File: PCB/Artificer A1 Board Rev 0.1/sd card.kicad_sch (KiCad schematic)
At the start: 1 part

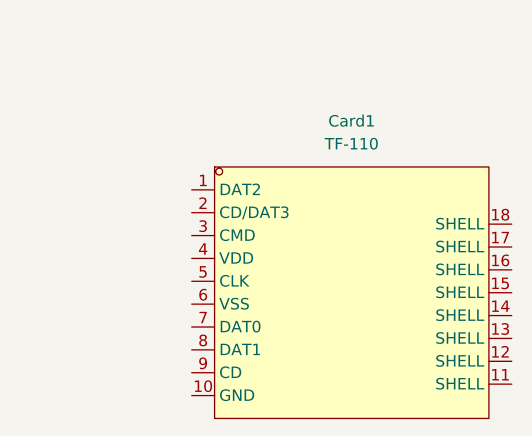
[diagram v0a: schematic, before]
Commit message: localized libraries
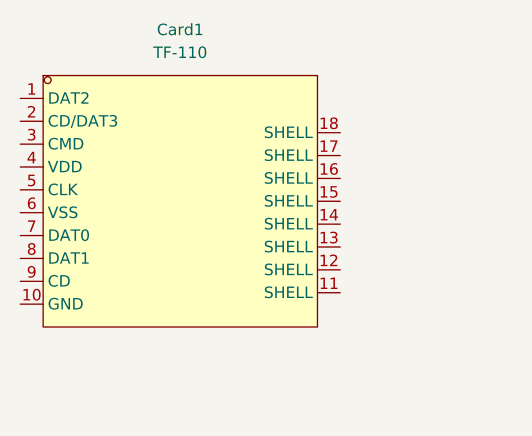
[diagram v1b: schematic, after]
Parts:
- removed Card1: TF-110, easyeda2kicad:TF-SMD_TF-110, symbol easyeda2kicad:TF-110
- added Card1: TF-110, easyeda:TF-SMD_TF-110, symbol easyeda:TF-110
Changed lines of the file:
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@@
 	)
 	(symbol
-		(lib_id "easyeda2kicad:TF-110")
-		(at 157.48 109.22 0)
+		(lib_id "easyeda:TF-110")
+		(at 138.43 99.06 0)
 		(unit 1)
 		(exclude_from_sim no)
@@
 		(fields_autoplaced yes)
 		(property "Reference" "Card1"
-			(at 157.48 90.17 0)
+			(at 138.43 80.01 0)
 			(effects
 				(font
@@
 		)
 		(property "Value" "TF-110"
-			(at 157.48 92.71 0)
+			(at 138.43 82.55 0)
 			(effects
 				(font
@@
 			)
 		)
-		(property "Footprint" "easyeda2kicad:TF-SMD_TF-110"
-			(at 157.48 128.27 0)
+		(property "Footprint" "easyeda:TF-SMD_TF-110"
+			(at 138.43 118.11 0)
 			(effects
 				(font
@@
 		)
 		(property "Datasheet" "https://lcsc.com/product-detail/Connector-Card-Sockets_XUNPU-TF-110_C266613.html"
-			(at 157.48 130.81 0)
+			(at 138.43 120.65 0)
 			(effects
 				(font
@@
 		)
 		(property "Description" ""
-			(at 157.48 109.22 0)
+			(at 138.43 99.06 0)
 			(effects
 				(font
@@
 		)
 		(property "LCSC Part" "C266613"
-			(at 157.48 133.35 0)
+			(at 138.43 123.19 0)
 			(effects
 				(font
@@
 			)
 		)
-		(pin "12"
+		(pin "1"
 		)
-		(pin "15"
+		(pin "4"
+		)
+		(pin "6"
+		)
+		(pin "2"
 		)
 		(pin "3"
 		)
-		(pin "11"
-		)
-		(pin "4"
+		(pin "16"
 		)
 		(pin "5"
 		)
-		(pin "16"
+		(pin "7"
 		)
-		(pin "2"
+		(pin "9"
 		)
 		(pin "8"
@@
 		(pin "10"
 		)
-		(pin "17"
+		(pin "18"
+		)
+		(pin "15"
 		)
 		(pin "13"
 		)
-		(pin "1"
-		)
-		(pin "18"
-		)
 		(pin "14"
 		)
-		(pin "6"
+		(pin "12"
 		)
-		(pin "9"
+		(pin "11"
 		)
-		(pin "7"
+		(pin "17"
 		)
 		(instances

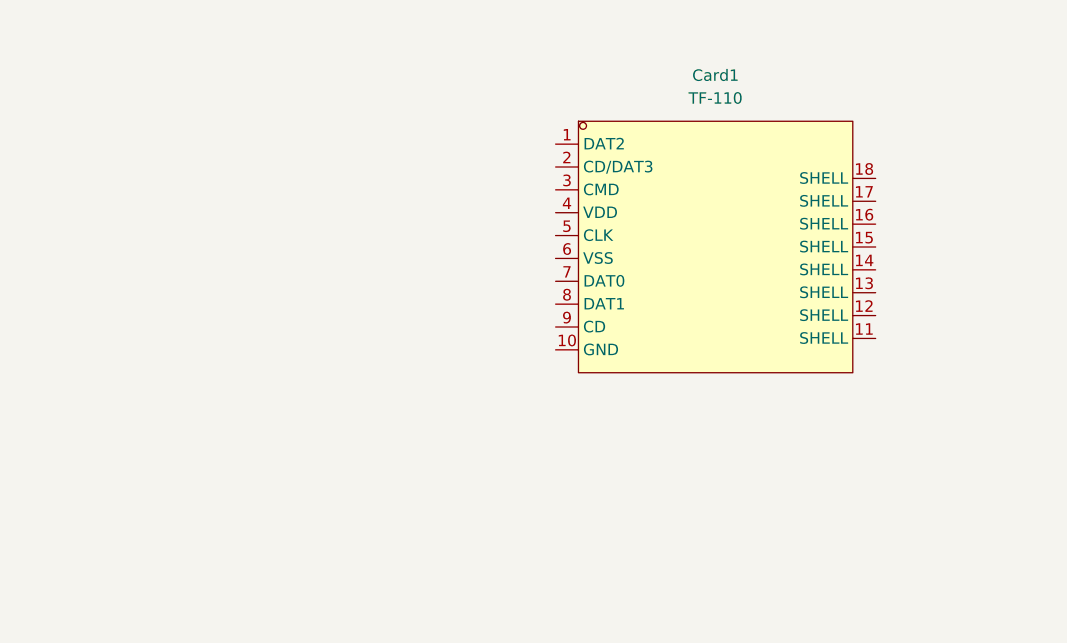
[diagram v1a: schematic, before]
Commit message: added: sd, wifi, audio, started power, fixed buses
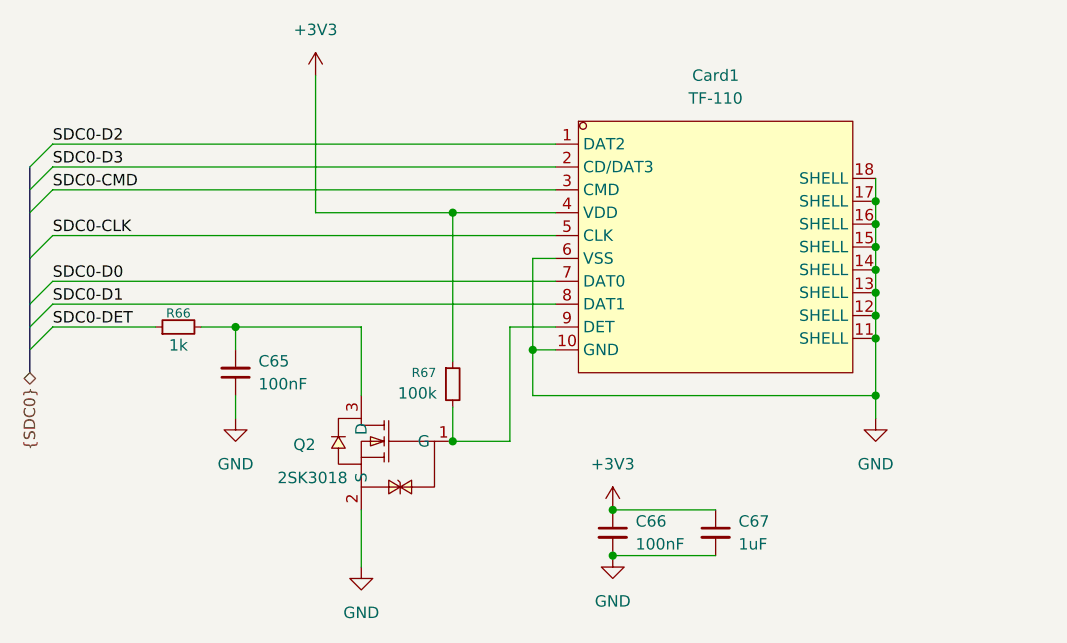
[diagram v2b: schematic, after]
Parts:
- added C65, C66: 100nF, symbol Device:C_Small
- added C67: 1uF, symbol Device:C_Small
- added Q2: 2SK3018, easyeda:SOT-23-3_L2.9-W1.4-P1.90-LS2.6-BR, symbol easyeda:2SK3018_C727148
- added R66: 1k, symbol Device:R_Small
- added R67: 100k, symbol Device:R_Small
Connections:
- net SDC0-D2: now reaches Card1.1 (DAT2)
- net GND: now reaches Card1.10 (GND)
- net GND: now also Card1.11 (SHELL), Card1.12 (SHELL), Card1.13 (SHELL), Card1.14 (SHELL), Card1.15 (SHELL), Card1.16 (SHELL), Card1.17 (SHELL), Card1.18 (SHELL), Card1.6 (VSS), C65.1, C66.2, C67.2, Q2.2 (S)
- net SDC0-D3: now reaches Card1.2 (CD/DAT3)
- net SDC0-CMD: now reaches Card1.3 (CMD)
- net +3V3: now reaches Card1.4 (VDD)
- net +3V3: now also C66.1, C67.1, R67.1
- net SDC0-CLK: now reaches Card1.5 (CLK)
- net SDC0-D0: now reaches Card1.7 (DAT0)
- net SDC0-D1: now reaches Card1.8 (DAT1)
- net at Card1.9 (DET): now also Q2.1 (G), R67.2
- new net: C65.2, Q2.3 (D), R66.2
- new net SDC0-DET: R66.1
